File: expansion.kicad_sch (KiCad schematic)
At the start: 11 parts

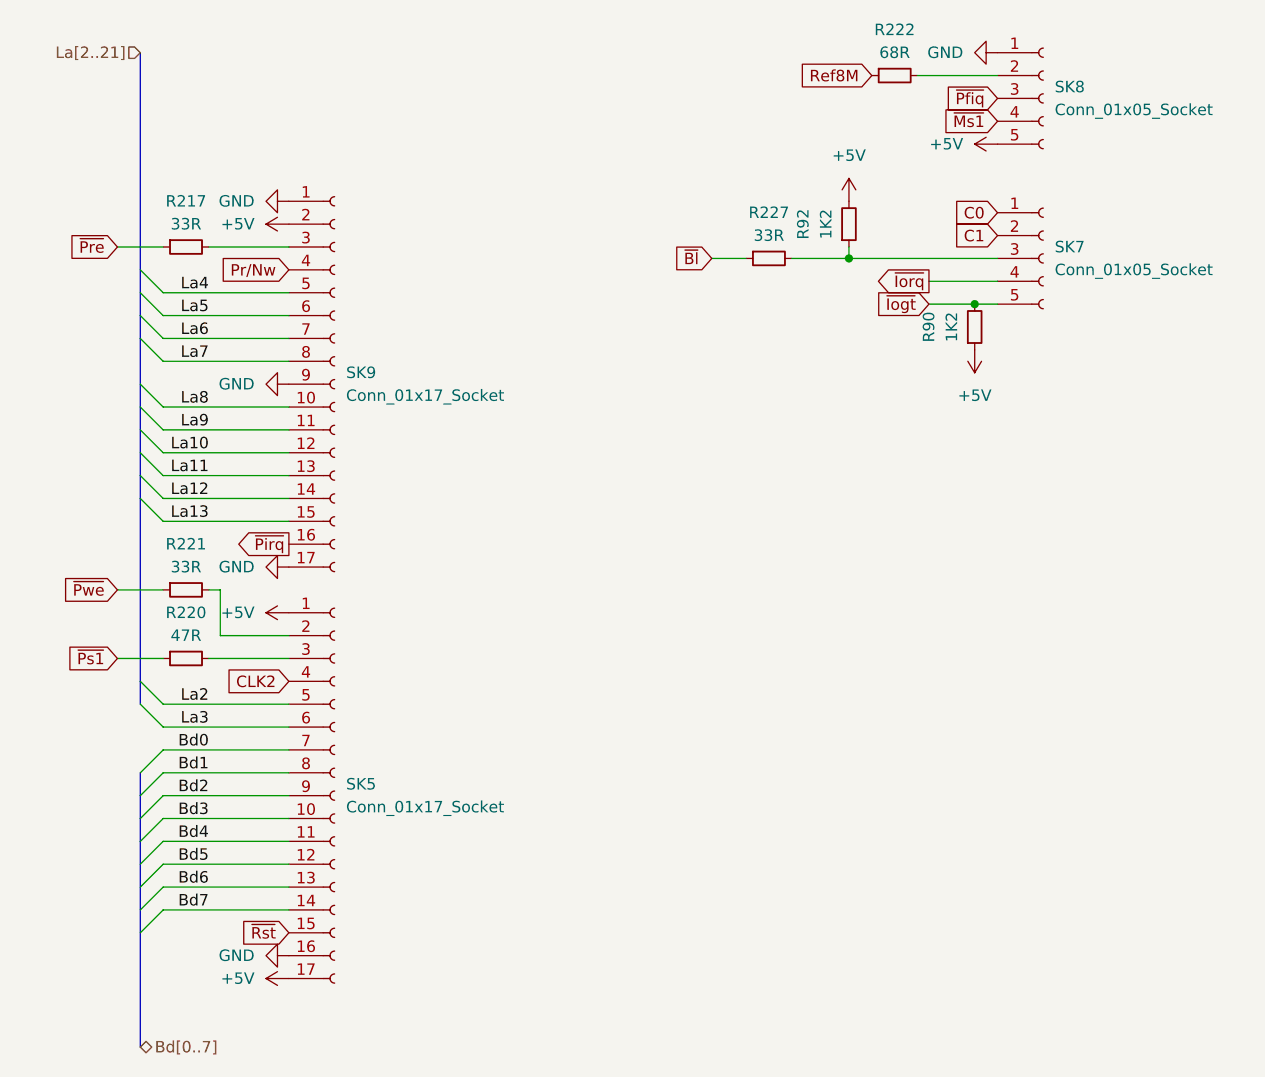
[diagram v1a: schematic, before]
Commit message: add ide and rework onboard ram
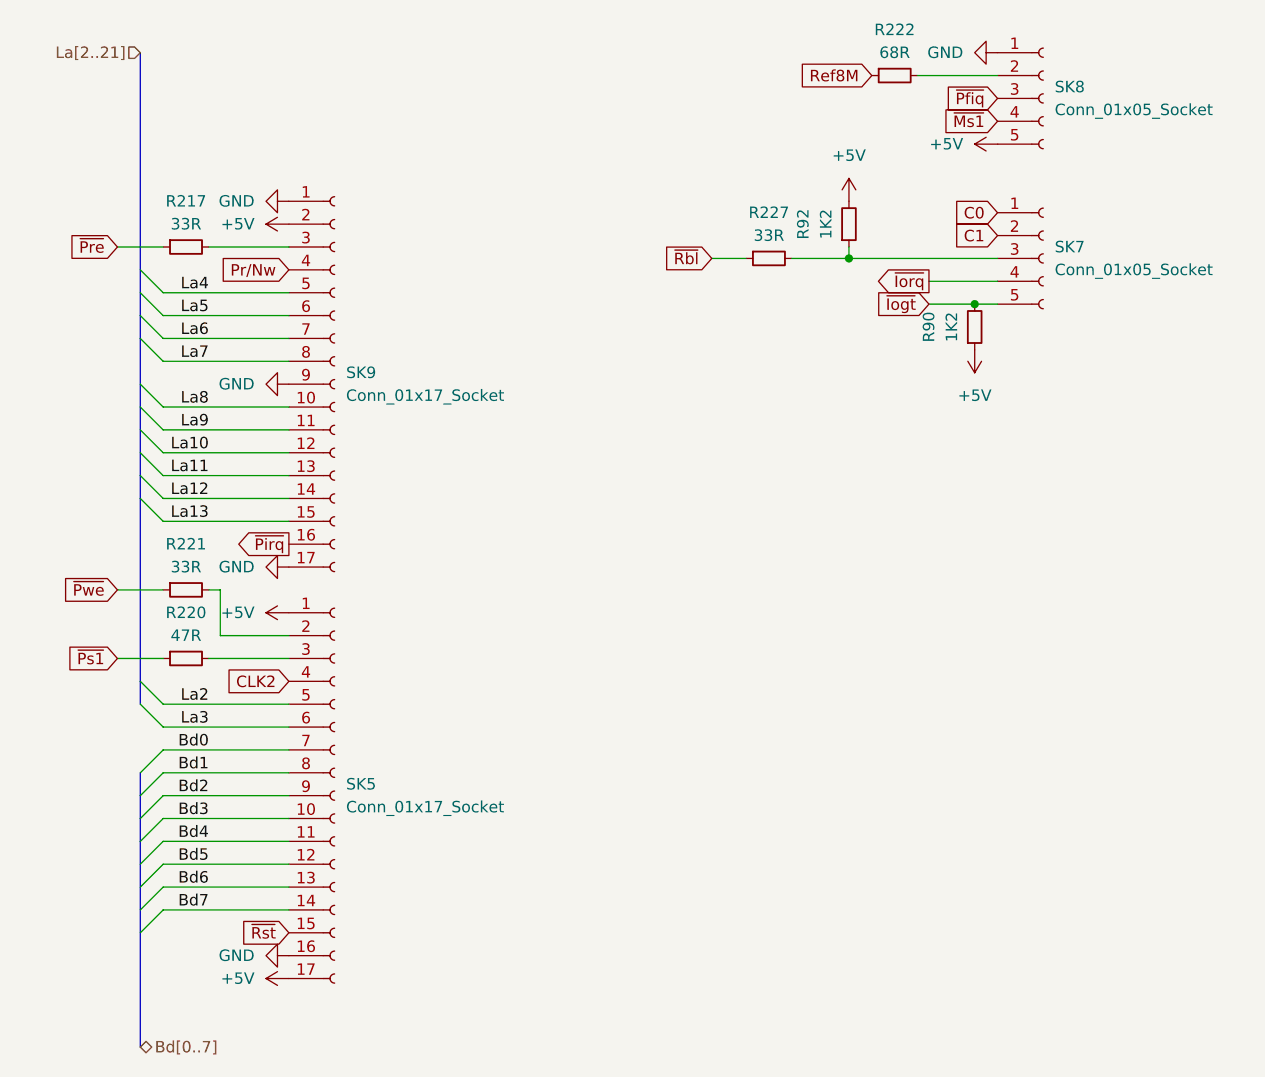
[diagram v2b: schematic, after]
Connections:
- net ~{Bl} renamed ~{Rbl}
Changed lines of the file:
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@@
 (kicad_sch
-	(version 20231120)
+	(version 20250114)
 	(generator "eeschema")
-	(generator_version "8.0")
+	(generator_version "9.0")
 	(paper "A4")
 	(junction
@@
 		)
 	)
-	(global_label "~{Bl}"
+	(global_label "~{Rbl}"
 		(shape input)
 		(at 142.24 57.15 180)
@@
 		)
 		(property "Intersheetrefs" "${INTERSHEET_REFS}"
-			(at 137.3196 57.15 0)
+			(at 136.1706 57.15 0)
 			(effects
 				(font
@@
 		)
 		(instances
-			(project ""
+			(project "Acorn-A3010"
 				(path "/999882f3-94f8-4a89-9093-27a47d0cb289/a81e918c-e432-436c-a2d0-ede42e8b201e"
 					(reference "SK5")
@@
 		)
 		(instances
-			(project ""
+			(project "Acorn-A3010"
 				(path "/999882f3-94f8-4a89-9093-27a47d0cb289/a81e918c-e432-436c-a2d0-ede42e8b201e"
 					(reference "SK8")
@@
 		)
 		(instances
-			(project ""
+			(project "Acorn-A3010"
 				(path "/999882f3-94f8-4a89-9093-27a47d0cb289/a81e918c-e432-436c-a2d0-ede42e8b201e"
 					(reference "#PWR084")
@@
 		)
 		(instances
-			(project ""
+			(project "Acorn-A3010"
 				(path "/999882f3-94f8-4a89-9093-27a47d0cb289/a81e918c-e432-436c-a2d0-ede42e8b201e"
 					(reference "#PWR082")
